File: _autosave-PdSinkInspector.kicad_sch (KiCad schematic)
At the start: 34 parts, among them IC1 632723100011, IC2 STUSB4700YQTR, IC3 632723100011, SW1 SW_Omron_B3FS, U1 RP2040, U2 W25Q128JVS, U3 TLV75733PDBV, Y1 ABMM2-12.000MHZ-E2-T

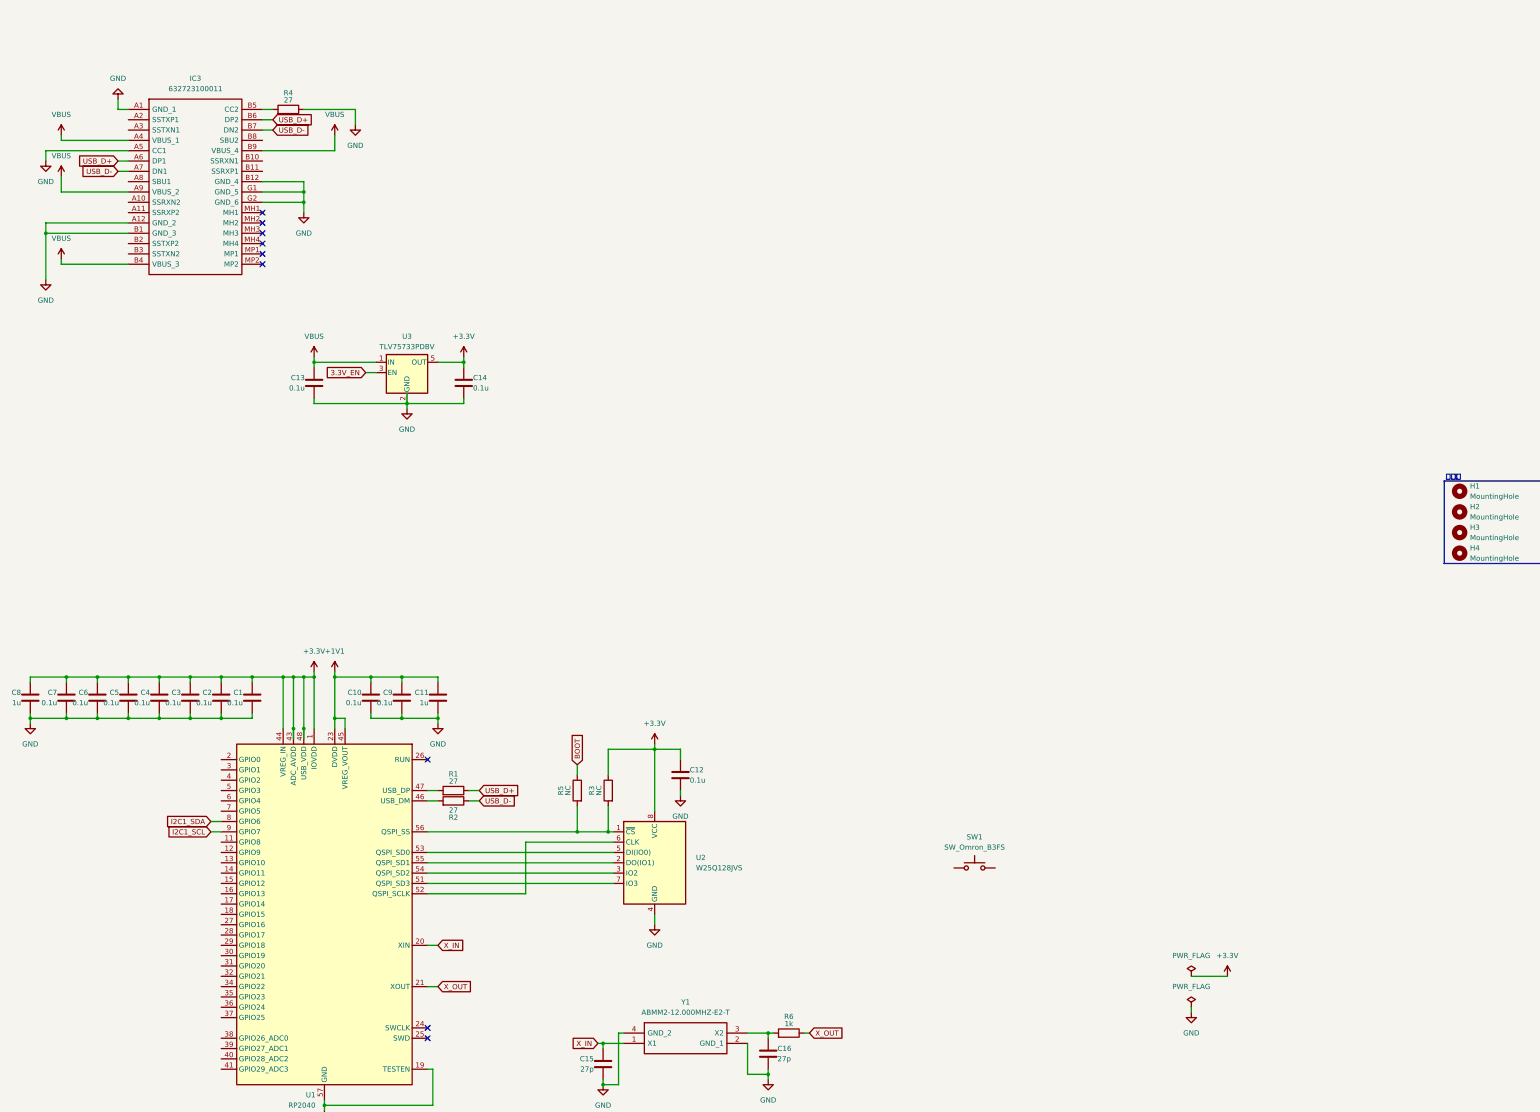
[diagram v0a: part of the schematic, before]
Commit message: LDO、Flash追加
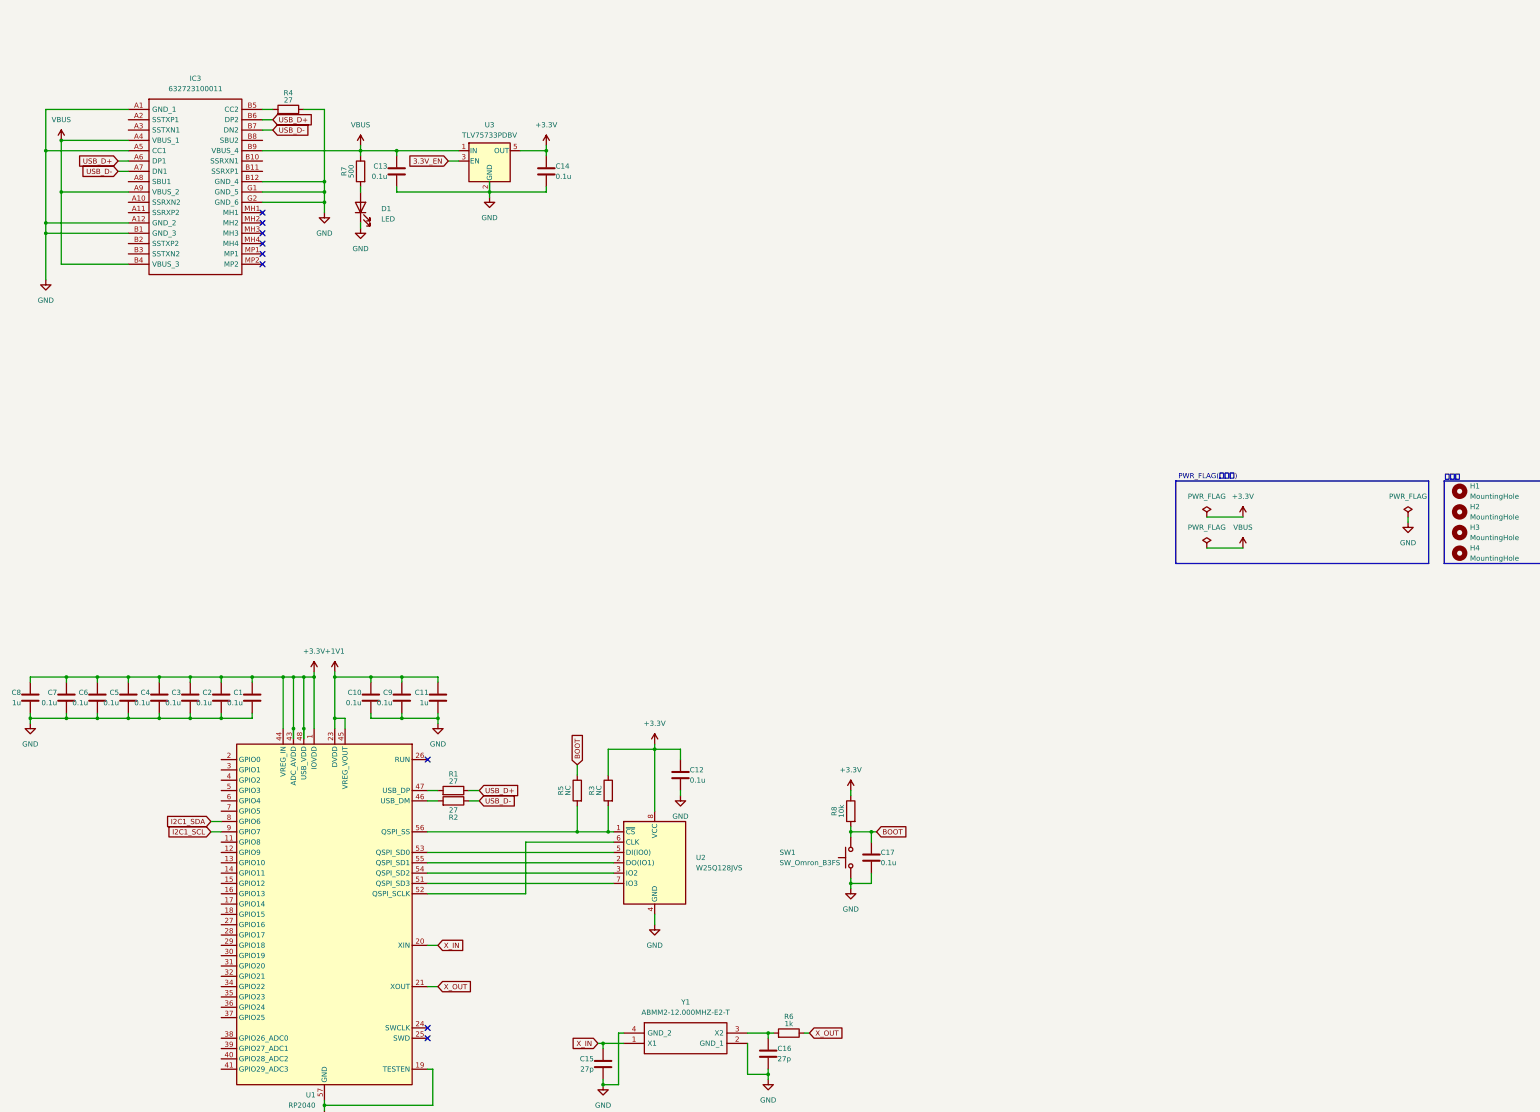
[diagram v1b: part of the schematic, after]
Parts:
- added C17: 0.1u, Capacitor_SMD:C_0603_1608Metric, symbol Device:C
- added D1: LED, LED_SMD:LED_0603_1608Metric, symbol Device:LED
- added R7: 500, Resistor_SMD:R_0603_1608Metric, symbol Device:R
- added R8: 10k, Resistor_SMD:R_0603_1608Metric, symbol Device:R
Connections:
- net +3.3V: now also R8.1
- net BOOT: now also SW1.2, C17.1, R8.2
- net GND: now also SW1.1, C17.2, D1.1 (K)
- net VBUS: now also R7.1
- new net: D1.2 (A), R7.2
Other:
- note added: "PWR_FLAG(お作法)"
- moved on the sheet: C13, C14, SW1, U3
